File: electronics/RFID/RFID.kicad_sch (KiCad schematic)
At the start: 8 parts, among them P1 UART_Connector

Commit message: hallo allemaal, dit is de meest recente versie van het KiCad project. Hopelijk snappen jullie mijn aanpassingen zodat we de samenwerking goed kunnen verderzetten. Groetjes van jullie teamgenoot, Robbe De Voet
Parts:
- added U2: ~, own:devkit_mount, symbol own:devkit_connector
- gave numbers to parts that had none: 1
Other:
- note added: "Schmitt trigger input LCD"

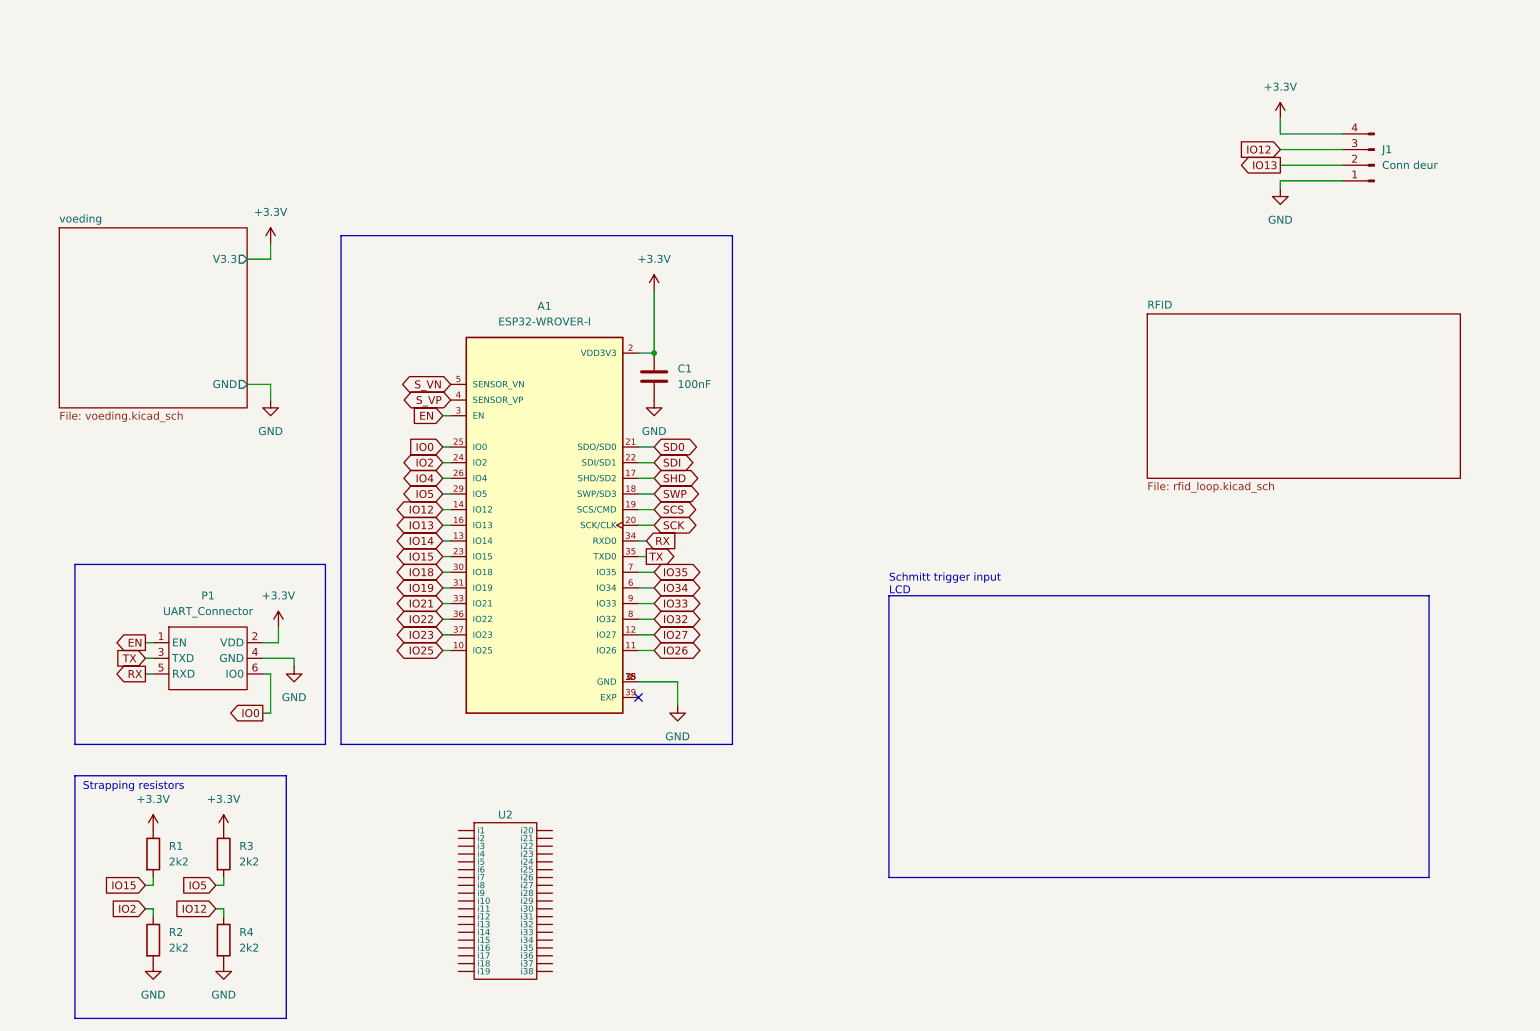
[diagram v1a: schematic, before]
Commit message: added tcp connection and device tab
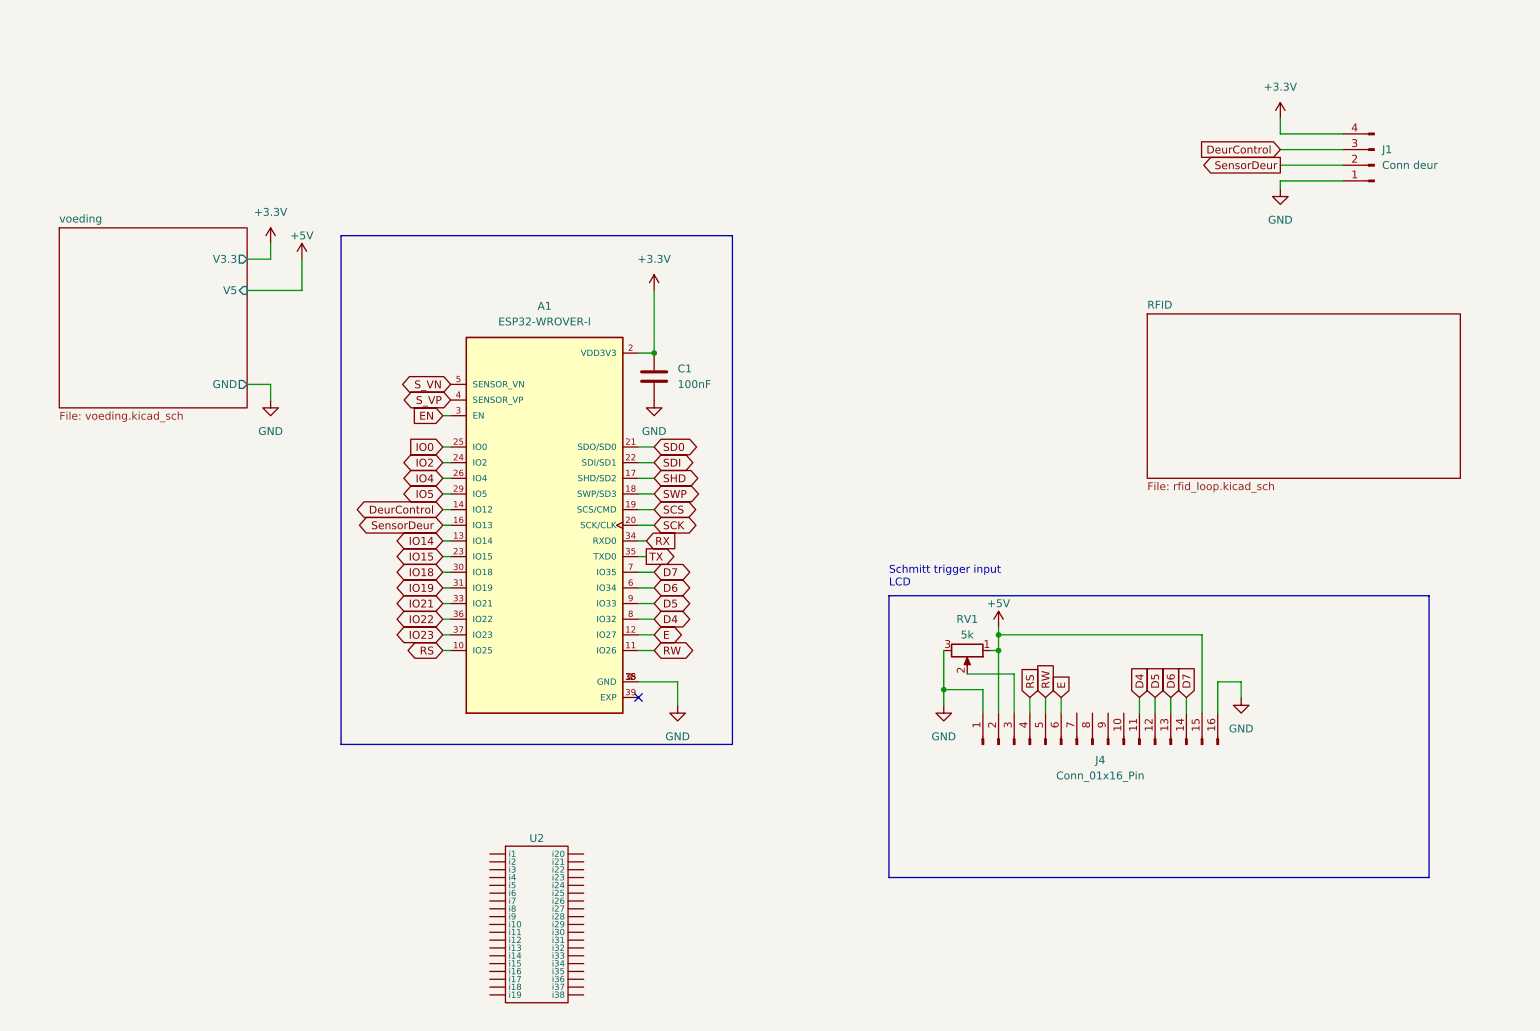
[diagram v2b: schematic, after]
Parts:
- removed P1: UART_Connector, UGent_standard_stock_Connector:UART_100mil, symbol custom:UART_Connector
- removed R1, R2, R3, R4: 2k2, Resistor_SMD:R_0805_2012Metric, symbol Device:R
- added J4: Conn_01x16_Pin, symbol Connector:Conn_01x16_Pin
- added RV1: 5k, symbol Device:R_Potentiometer
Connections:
- net GND: now also J4.1 (Pin_1), J4.16 (Pin_16), RV1.3
- net IO12 renamed DeurControl
- net IO13 renamed SensorDeur
- net IO25 renamed RS
- net RS: now also J4.4 (Pin_4)
- net IO26 renamed RW
- net RW: now also J4.5 (Pin_5)
- net IO27 renamed E
- net E: now also J4.6 (Pin_6)
- net IO32 renamed D4
- net D4: now also J4.11 (Pin_11)
- net IO33 renamed D5
- net D5: now also J4.12 (Pin_12)
- net IO34 renamed D6
- net D6: now also J4.13 (Pin_13)
- net IO35 renamed D7
- net D7: now also J4.14 (Pin_14)
- new net: J4.3 (Pin_3), RV1.2
- new net +5V: J4.15 (Pin_15), J4.2 (Pin_2), RV1.1
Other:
- sheet voeding ports: added V5; removed none
- note removed: "Strapping resistors"
- moved on the sheet: U2

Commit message: schematic
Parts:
- removed A1: ESP32-WROVER-I, UGent_standard_stock_IC:XCVR_ESP32-WROVER-I, symbol UGent_standard_stock_IC:ESP32-WROVER-I
- removed J1: Conn deur, Connector_PinHeader_2.54mm:PinHeader_1x04_P2.54mm_Vertical, symbol UGent_standard_stock_Connector:Conn_01x04_2,54mm
- removed U2: ~, own:devkit_mount, symbol own:devkit_connector
- added C2: 10µF, Capacitor_SMD:C_0805_2012Metric, symbol Device:C
- added C3: 100nF, Capacitor_SMD:C_0805_2012Metric, symbol Device:C
- added C4, C5: 22µF, Capacitor_SMD:C_0805_2012Metric, symbol Device:C
- added J1: USB_C_Receptacle_PowerOnly_6P, UGent_standard_stock_Connector:USB_C_Receptacle_GCT_USB4135-GF-A_6P_TopMnt_Horizontal, symbol UGent_standard_stock_Connector:USB_C_Receptacle_PowerOnly_6P
- added J5: Conn_01x08_Pin, Connector_PinSocket_2.54mm:PinSocket_1x08_P2.54mm_Vertical, symbol Connector:Conn_01x08_Pin
- added L1: 3.9µH, Inductor_SMD:L_Bourns-SRN6028, symbol Device:L
- added R1: 0, Resistor_SMD:R_0805_2012Metric, symbol Device:R
- added R2: 5K1, Resistor_SMD:R_0805_2012Metric, symbol Device:R
- added R3: 5k1, Resistor_SMD:R_0805_2012Metric, symbol Device:R
- added U1: AP63200WU, Package_TO_SOT_SMD:TSOT-23-6, symbol UGent_standard_stock_Power:AP63200WU
- added U2: 74LVC2G14, Package_TO_SOT_SMD:SOT-23-6, symbol 74xGxx:74LVC2G14
- added U3: ~, Library:espConn, symbol goot:ESP32
- J4: footprint (none) -> Connector_PinSocket_2.54mm:PinSocket_1x16_P2.54mm_Vertical
- RV1: footprint (none) -> Potentiometer_SMD:Potentiometer_Bourns_3214W_Vertical
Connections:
- net +3.3V: now also J5.8 (Pin_8), U2.5 (VCC), U3.1 (3V3)
- net +5V: now also C2.1, J1.A9 (VBUS), J1.B9 (VBUS), U1.2 (EN), U1.3 (IN)
- net D4: now also U3.31 (16)
- net D5: now also U3.30 (17)
- net D6: now also U3.29 (5)
- net D7: now also U3.28 (18)
- net DeurControl: now also J5.3 (Pin_3), U3.27 (19)
- net E: now also U3.17 (D3)
- net GND: now also C2.2, C4.2, C5.2, J1.A12 (GND), J1.B12 (GND), J5.1 (Pin_1), R1.2, R2.2, R3.2, U1.4 (GND), U2.2 (GND), U3.14 (GND), U3.20 (GND), U3.26 (GND)
- net RS: now also U3.15 (13)
- net RW: now also U3.16 (D2)
- net RX: now also J5.7 (Pin_7), U3.24 (RX)
- net SensorDeur: now also J5.2 (Pin_2), U3.25 (21)
- net TX: now also J5.6 (Pin_6), U3.23 (TX)
- net D3: now reaches J4.10 (Pin_10)
- net D3: now also U3.32 (4)
- net D0: now reaches J4.7 (Pin_7)
- net D0: now also U3.35 (D15)
- net D1: now reaches J4.8 (Pin_8)
- net D1: now also U3.34 (2)
- net D2: now reaches J4.9 (Pin_9)
- net D2: now also U3.33 (0)
- new net: J1.S1 (SHIELD), R1.1
- new net: J5.4 (Pin_4), U2.3
- new net: J5.5 (Pin_5), U2.1
- new net: J1.A5 (CC1), R2.1
- new net: J1.B5 (CC2), R3.1
- new net: C3.1, L1.1, U1.5 (SW)
- new net: C3.2, U1.6 (BST)
- new net M1: U2.6, U3.21 (23)
- new net M2: U2.4, U3.22
- new net V3.3: C4.1, C5.1, L1.2, U1.1 (FB)
- no-connect marks 1 -> 0
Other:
- removed sheet RFID
- removed sheet voeding
- note added: "5v to 3.3v buck converter"
- note added: "ESP32"
- note added: "IO"
- note added: "LCD"
- note removed: "Schmitt trigger input LCD"
- moved on the sheet: C1, J4, RV1

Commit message: added basic pcb
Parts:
- removed J5: Conn_01x08_Pin, Connector_PinSocket_2.54mm:PinSocket_1x08_P2.54mm_Vertical, symbol Connector:Conn_01x08_Pin
- removed R1: 0, Resistor_SMD:R_0805_2012Metric, symbol Device:R
- added H1, H2, H3, H4: MountingHole, MountingHole:MountingHole_4mm, symbol Mechanical:MountingHole
- added J2: Conn_01x10_Pin, Connector_PinSocket_2.54mm:PinSocket_1x10_P2.54mm_Vertical, symbol Connector:Conn_01x10_Pin
- added JP1: Jumper_2_Open, Jumper:SolderJumper-2_P1.3mm_Open_TrianglePad1.0x1.5mm, symbol Jumper:Jumper_2_Open
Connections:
- net +3.3V: now also J2.9 (Pin_9)
- net +5V: now also J2.10 (Pin_10)
- net D0: now also U3.9 (25); no longer U3.35 (D15)
- net D1: now also U3.10 (26); no longer U3.34 (2)
- net D2: now also U3.11 (27); no longer U3.33 (0)
- net D3: now also U3.12 (14); no longer U3.32 (4)
- net D4: now also U3.13 (12); no longer U3.31 (16)
- net D5: now also U3.15 (13); no longer U3.30 (17)
- net D6: now also U3.16 (D2); no longer U3.29 (5)
- net D7: now also U3.17 (D3); no longer U3.28 (18)
- net DeurControl: now also J2.6 (Pin_6)
- net E: now also U3.8 (33); no longer U3.17 (D3)
- net GND: now also J2.1 (Pin_1), J2.2 (Pin_2), JP1.2 (B)
- net M1: now also U3.34 (2); no longer U3.21 (23)
- net M2: now also U3.33 (0); no longer U3.22
- net RS: now also U3.6 (35); no longer U3.15 (13)
- net RW: now also U3.7 (32); no longer U3.16 (D2)
- net RX: now also J2.4 (Pin_4)
- net SensorDeur: now also J2.5 (Pin_5)
- net TX: now also J2.3 (Pin_3)
- net at J1.S1 (SHIELD): now also JP1.1 (A)
- net at U2.3: now also J2.7 (Pin_7)
- net at U2.1: now also J2.8 (Pin_8)

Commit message: pcb
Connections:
- net V3.3 is gone; now on net +3.3V: C4.1, C5.1, L1.2, U1.1 (FB)
- net +3.3V: now also U3.2 (EN)
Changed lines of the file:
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@@
   (junction (at 74.93 86.36) (diameter 0) (color 0 0 0 0)
   )
+  (junction (at 119.38 43.18) (diameter 0) (color 0 0 0 0)
+  )
   (junction (at 74.93 90.17) (diameter 0) (color 0 0 0 0)
   )
@@
     (stroke (width 0) (type default))
   )
-  (wire (pts (xy 77.47 74.93) (xy 74.93 74.93))
-    (stroke (width 0) (type default))
-  )
   (wire (pts (xy 31.75 62.23) (xy 31.75 59.69))
     (stroke (width 0) (type default))
@@
   )
   (wire (pts (xy 153.67 35.56) (xy 153.67 33.02))
+    (stroke (width 0) (type default))
+  )
+  (wire (pts (xy 119.38 43.18) (xy 119.38 45.72))
+    (stroke (width 0) (type default))
+  )
+  (wire (pts (xy 119.38 45.72) (xy 120.65 45.72))
     (stroke (width 0) (type default))
   )
@@
   )
   (hierarchical_label "GND" (shape output) (at 77.47 99.06 0) (fields_autoplaced)
-    (effects (font (size 1.27 1.27)) (justify left))
-  )
-  (hierarchical_label "V3.3" (shape output) (at 77.47 74.93 0) (fields_autoplaced)
     (effects (font (size 1.27 1.27)) (justify left))
   )
@@
         )
       )
+    )
+  )
+  (symbol (lib_id "power:+3.3V") (at 74.93 74.93 0) (unit 1)
+    (in_bom yes) (on_board yes) (dnp no) (fields_autoplaced)
+    (property "Reference" "#PWR021" (at 74.93 78.74 0)
+      (effects (font (size 1.27 1.27)) hide)
+    )
+    (property "Value" "+3.3V" (at 74.93 69.85 0)
+      (effects (font (size 1.27 1.27)))
+    )
+    (property "Footprint" "" (at 74.93 74.93 0)
+      (effects (font (size 1.27 1.27)) hide)
+    )
+    (property "Datasheet" "" (at 74.93 74.93 0)
+      (effects (font (size 1.27 1.27)) hide)
+    )
+    (pin "1")
+    (instances
+      (project "RFID"
+        (path "/e1bf2693-f20d-4944-8ac7-30b938532662"
+          (reference "#PWR021") (unit 1)
+        )
+      )

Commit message: pcbV2
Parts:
- removed J2: Conn_01x10_Pin, Connector_PinSocket_2.54mm:PinSocket_1x10_P2.54mm_Vertical, symbol Connector:Conn_01x10_Pin
- added J2: Conn deur, Connector_PinHeader_2.54mm:PinHeader_1x04_P2.54mm_Vertical, symbol Connector:Conn_01x04_Pin
- added J3: Conn Uart, Connector_PinHeader_2.54mm:PinHeader_1x04_P2.54mm_Vertical, symbol Connector:Conn_01x04_Pin
- added J5: Conn motion, Connector_PinHeader_2.54mm:PinHeader_1x04_P2.54mm_Vertical, symbol Connector:Conn_01x04_Pin
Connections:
- net +3.3V: now also J2.4 (Pin_4), J3.4 (Pin_4)
- net +5V: now also J5.4 (Pin_4)
- net D0: now also U3.30 (17); no longer U3.9 (25)
- net D1: now also U3.28 (18); no longer U3.10 (26)
- net D2: now also U3.27 (19); no longer U3.11 (27)
- net D3: now also U3.25 (21); no longer U3.12 (14)
- net D4: now also U3.24 (RX); no longer U3.13 (12)
- net D5: now also U3.23 (TX); no longer U3.15 (13)
- net D6: now also U3.22; no longer U3.16 (D2)
- net D7: now also U3.21 (23); no longer U3.17 (D3)
- net DeurControl: now also U3.9 (25), J2.3 (Pin_3); no longer U3.27 (19)
- net E: now also U3.31 (16); no longer U3.8 (33)
- net GND: now also J2.1 (Pin_1), J3.1 (Pin_1), J5.1 (Pin_1)
- net M1: now also U3.7 (32); no longer U3.34 (2)
- net M2: now also U3.8 (33); no longer U3.33 (0)
- net RS: now also U3.34 (2); no longer U3.6 (35)
- net RW: now also U3.32 (4); no longer U3.7 (32)
- net RX: now also U3.12 (14), J3.3 (Pin_3); no longer U3.24 (RX)
- net SensorDeur: now also U3.10 (26), J2.2 (Pin_2); no longer U3.25 (21)
- net TX: now also U3.13 (12), J3.2 (Pin_2); no longer U3.23 (TX)
- net at U2.3: now also J5.2 (Pin_2)
- net at U2.1: now also J5.3 (Pin_3)
- no-connect marks 0 -> 16
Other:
- moved on the sheet: C1, H3, H4

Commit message: pcbVfinal?
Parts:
- J3: footprint Connector_PinHeader_2.54mm:PinHeader_1x04_P2.54mm_Vertical -> Connector_PinHeader_2.00mm:PinHeader_1x04_P2.00mm_Vertical
- U1: value AP63200WU -> AP63202WU
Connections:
- net +3.3V: no longer J3.4 (Pin_4)
- net +5V: now also J3.2 (Pin_2)
- net RX: now also J3.4 (Pin_4); no longer J3.3 (Pin_3)
- net TX: now also J3.3 (Pin_3); no longer J3.2 (Pin_2)
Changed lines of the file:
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@@
+    (stroke (width 0) (type default))
+  )
+  (wire (pts (xy 242.57 80.01) (xy 245.11 80.01))
     (stroke (width 0) (type default))
   )
@@
     (stroke (width 0) (type default))
   )
-  (wire (pts (xy 242.57 80.01) (xy 245.11 80.01))
-    (stroke (width 0) (type default))
-  )
   (wire (pts (xy 229.87 140.97) (xy 229.87 143.51))
     (stroke (width 0) (type default))
@@
     (stroke (width 0) (type default))
   )
-  (wire (pts (xy 245.11 77.47) (xy 242.57 77.47))
-    (stroke (width 0) (type default))
-  )
-  (wire (pts (xy 242.57 82.55) (xy 245.11 82.55))
-    (stroke (width 0) (type default))
-  )
   (wire (pts (xy 198.12 142.24) (xy 198.12 139.7))
     (stroke (width 0) (type default))
@@
     (stroke (width 0) (type default))
   )
+  (wire (pts (xy 240.03 82.55) (xy 245.11 82.55))
+    (stroke (width 0) (type default))
+  )
   (wire (pts (xy 33.02 59.69) (xy 31.75 59.69))
     (stroke (width 0) (type default))
@@
     (stroke (width 0) (type default))
   )
+  (wire (pts (xy 242.57 77.47) (xy 245.11 77.47))
+    (stroke (width 0) (type default))
+  )
   (wire (pts (xy 224.79 140.97) (xy 224.79 143.51))
     (stroke (width 0) (type default))
@@
   )
   (wire (pts (xy 238.76 45.72) (xy 240.03 45.72))
-    (stroke (width 0) (type default))
-  )
-  (wire (pts (xy 242.57 77.47) (xy 242.57 76.2))
     (stroke (width 0) (type default))
   )
@@
     )
   )
-  (global_label "TX" (shape input) (at 242.57 82.55 180) (fields_autoplaced)
+  (global_label "TX" (shape input) (at 242.57 80.01 180) (fields_autoplaced)
     (effects (font (size 1.27 1.27)) (justify right))
-    (property "Intersheetrefs" "${INTERSHEET_REFS}" (at 237.4871 82.55 0)
+    (property "Intersheetrefs" "${INTERSHEET_REFS}" (at 237.4871 80.01 0)
       (effects (font (size 1.27 1.27)) (justify right) hide)
     )
   )
-  (global_label "RX" (shape output) (at 242.57 80.01 180) (fields_autoplaced)
+  (global_label "RX" (shape output) (at 242.57 77.47 180) (fields_autoplaced)
     (effects (font (size 1.27 1.27)) (justify right))
-    (property "Intersheetrefs" "${INTERSHEET_REFS}" (at 237.1847 80.01 0)
+    (property "Intersheetrefs" "${INTERSHEET_REFS}" (at 237.1847 77.47 0)
       (effects (font (size 1.27 1.27)) (justify right) hide)
     )
@@
         (path "/e1bf2693-f20d-4944-8ac7-30b938532662"
           (reference "JP1") (unit 1)
-        )
-      )
-    )
-  )
-  (symbol (lib_id "power:+3.3V") (at 242.57 76.2 0) (unit 1)
-    (in_bom yes) (on_board yes) (dnp no) (fields_autoplaced)
-    (property "Reference" "#PWR05" (at 242.57 80.01 0)
-      (effects (font (size 1.27 1.27)) hide)
-    )
-    (property "Value" "+3.3V" (at 242.57 72.39 0)
-      (effects (font (size 1.27 1.27)))
-    )
-    (property "Footprint" "" (at 242.57 76.2 0)
-      (effects (font (size 1.27 1.27)) hide)
-    )
-    (property "Datasheet" "" (at 242.57 76.2 0)
-      (effects (font (size 1.27 1.27)) hide)
-    )
-    (pin "1")
-    (instances
-      (project "RFID"
-        (path "/e1bf2693-f20d-4944-8ac7-30b938532662"
-          (reference "#PWR05") (unit 1)
         )
       )
@@
       (effects (font (size 1.27 1.27)) (justify right))
     )
-    (property "Footprint" "Connector_PinHeader_2.54mm:PinHeader_1x04_P2.54mm_Vertical" (at 250.19 82.55 0)
+    (property "Footprint" "Connector_PinHeader_2.00mm:PinHeader_1x04_P2.00mm_Vertical" (at 250.19 82.55 0)
       (effects (font (size 1.27 1.27)) hide)
     )
@@
   (symbol (lib_id "UGent_standard_stock_Power:AP63200WU") (at 45.72 87.63 0) (unit 1)
     (in_bom yes) (on_board yes) (dnp no) (fields_autoplaced)
-    (property "Reference" "U1" (at 45.72 77.47 0)
-      (effects (font (size 1.27 1.27)))
-    )
-    (property "Value" "AP63200WU" (at 45.72 80.01 0)
+    (property "Reference" "U1" (at 45.72 78.74 0)
+      (effects (font (size 1.27 1.27)))
+    )
+    (property "Value" "AP63202WU" (at 45.72 81.28 0)
       (effects (font (size 1.27 1.27)))
     )
@@
         )
       )
+    )
+  )
+  (symbol (lib_id "power:+5V") (at 240.03 82.55 90) (unit 1)
+    (in_bom yes) (on_board yes) (dnp no)
+    (property "Reference" "#PWR05" (at 243.84 82.55 0)
+      (effects (font (size 1.27 1.27)) hide)
+    )
+    (property "Value" "+5V" (at 232.41 82.55 90)
+      (effects (font (size 1.27 1.27)) (justify right))
+    )
+    (property "Footprint" "" (at 240.03 82.55 0)
+      (effects (font (size 1.27 1.27)) hide)
+    )
+    (property "Datasheet" "" (at 240.03 82.55 0)
+      (effects (font (size 1.27 1.27)) hide)
+    )
+    (pin "1")
+    (instances
+      (project "RFID"
+        (path "/e1bf2693-f20d-4944-8ac7-30b938532662"
+          (reference "#PWR05") (unit 1)
+        )
+      )

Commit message: proxima fixed :chad:
fixed by proxi hihihiih love you <3
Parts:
- L1: footprint Inductor_SMD:L_Bourns-SRN6028 -> KiCad:SRR4828A3R9Y
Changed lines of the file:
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@@
       (effects (font (size 1.27 1.27)))
     )
-    (property "Footprint" "Inductor_SMD:L_Bourns-SRN6028" (at 68.58 78.74 0)
+    (property "Footprint" "KiCad:SRR4828A3R9Y" (at 68.58 78.74 0)
       (effects (font (size 1.27 1.27)) hide)
     )
